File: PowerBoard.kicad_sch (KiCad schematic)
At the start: 106 parts, among them IC1 LT1910ES8#PBF, IC2 LT1910ES8#PBF, IC3 LT1910ES8#PBF, IC4 LT1910ES8#PBF, J1 XT90, J10 DEAN_T, J11 DEAN_T, J12 DEAN_T, J13 DEAN_T, J14 DEAN_T, J15 DEAN_T, J16 XT60, J17 XT60, J18 XT60, J19 XT60, J2 DEAN_T, J20 XT60, J21 XT60, J22 XT30, J23 XT30, J24 XT30, J25 XT30, J26 XT30, J27 XT30, J28 XT90, J29 XT30, J3 XT60, J30 XT30, J31 XT30, J32 Conn_01x02, J4 XT30, J5 XT90, J6 XT90, J7 XT90, J8 XT90, J9 XT90, Q1 IRFS7437TRLPBF, Q2 IRFS7437TRLPBF, Q3 IRFS7437TRLPBF, Q5 IRFS7530-7PPBF, U1 Pico, U2 LM317_TO-220

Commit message: Finish the design
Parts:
- removed A1, A2: ADS1115_ADC_Module, my_footprint_lib:ADS1115, symbol Charleslabs_Parts:ADS1115_ADC_Module
- removed ADC1, SPI1: Screw_Terminal_01x04, TerminalBlock:TerminalBlock_Xinya_XY308-2.54-4P_1x04_P2.54mm_Horizontal, symbol Connector:Screw_Terminal_01x04
- removed C2: 1u, Capacitor_SMD:C_1206_3216Metric, symbol Device:C
- removed C3, C4: 10u, Capacitor_Tantalum_SMD:CP_EIA-7343-15_Kemet-W, symbol Device:C_Polarized
- removed J14: DEAN_T, my_footprint_lib:DEAN_T, symbol Connector_Generic:Conn_01x02
- removed J26: XT30, my_footprint_lib:XT30, symbol Connector_Generic:Conn_01x02
- removed J6: XT90, my_footprint_lib:XT90, symbol Connector_Generic:Conn_01x02
- removed Q5: IRFS7530-7PPBF, IRFS41157PPBF, symbol SamacSys_Parts:IRFS7530-7PPBF
- removed R25, R27, R29, R32: 100k, Resistor_SMD:R_1206_3216Metric, symbol Device:R_US
- removed R26, R28, R31: 10k, Resistor_SMD:R_1206_3216Metric, symbol Device:R_US
- removed R30: 33k, Resistor_SMD:R_1206_3216Metric, symbol Device:R_US
- removed R35: 680R, Resistor_SMD:R_1206_3216Metric, symbol Device:R_US
- removed R36: 220R, Resistor_SMD:R_1206_3216Metric, symbol Device:R_US
- removed U2: LM317_TO-220, Package_TO_SOT_THT:TO-220-3_Vertical, symbol Regulator_Linear:LM317_TO-220
- added C10: 22pF, Capacitor_SMD:C_1206_3216Metric, symbol Device:C
- added C11: 3300pF, Capacitor_SMD:C_1206_3216Metric, symbol Device:C
- added C12: 10u, Capacitor_SMD:C_1206_3216Metric, symbol Device:C
- added C13, C7, C8: 1u, Capacitor_SMD:C_1206_3216Metric, symbol Device:C
- added C9: 5.5nF, Capacitor_SMD:C_1206_3216Metric, symbol Device:C
- added D10: SMAJ30CA, Diode_SMD:D_SMA, symbol Diode:SMAJ30CA
- added D3, D6: LED, Diode_SMD:D_1206_3216Metric, symbol Device:LED
- added F1: Fuse, Fuse:Fuse_Blade_ATO_directSolder, symbol Device:Fuse
- added H5: MountingHole, MountingHole:MountingHole_3.2mm_M3, symbol Mechanical:MountingHole
- added IC1: LT1910ES8#PBF, SOIC127P599X175-8N, symbol SamacSys_Parts:LT1910ES8#PBF
- added IC7: MAX17541GATB+T, SON50P200X300X80-11N, symbol SamacSys_Parts:MAX17541GATB+T
- added J10: XT90, SamacSys_Parts:XT90, symbol Connector_Generic:Conn_01x02
- added J16: DEAN_T, SamacSys_Parts:DEANS-T, symbol Connector_Generic:Conn_01x02
- added J22, J41: XT60, Connector_AMASS:AMASS_XT60-F_1x02_P7.20mm_Vertical, symbol Connector_Generic:Conn_01x02
- added J32, J34, J35, J36, J37, J38, J39, J40: XT30, Connector_AMASS:AMASS_XT30U-F_1x02_P5.0mm_Vertical, symbol Connector_Generic:Conn_01x02
- added L1: 470M, SRR5828A2R6Y, symbol SamacSys_Parts:SRR5828A-470M
- added Q1: IRFS7530TRL7PP, IRFS7530TRL7PP, symbol SamacSys_Parts:IRFS7530TRL7PP
- added Q2: IRFS7437TRLPBF, Package_TO_SOT_SMD:TO-263-2, symbol Transistor_FET:IRF9540N
- added R16: 80k, Resistor_SMD:R_1206_3216Metric, symbol Device:R
- added R17: 17.5k, Resistor_SMD:R_1206_3216Metric, symbol Device:R
- added R18, R19, R20, R26, R27, R28, R29: 10k, Resistor_SMD:R_1206_3216Metric, symbol Device:R
- added R2, R5: 6k8, Resistor_SMD:R_1206_3216Metric, symbol Device:R_US
- added R21: 21.5k, Resistor_SMD:R_1206_3216Metric, symbol Device:R
- added R7: 5m, RESC3216X89N, symbol SamacSys_Parts:WSL12061L000FEA
- added U2, U3, U4, U5, U6: INA238, Package_SO:VSSOP-10_3x3mm_P0.5mm, symbol Sensor_Energy:INA238
- J1, J7, J8, J9: footprint my_footprint_lib:XT90 -> SamacSys_Parts:XT90
- J11, J12, J13: value DEAN_T -> XT90; footprint my_footprint_lib:DEAN_T -> SamacSys_Parts:XT90
- J14: renamed from J10; footprint my_footprint_lib:DEAN_T -> SamacSys_Parts:DEANS-T
- J15, J2: footprint my_footprint_lib:DEAN_T -> SamacSys_Parts:DEANS-T
- J17, J18, J19: value XT60 -> DEAN_T; footprint Connector_AMASS:AMASS_XT60-F_1x02_P7.20mm_Vertical -> SamacSys_Parts:DEANS-T
- J23, J24, J25, J27, J29, J30, J31: value XT30 -> XT60; footprint my_footprint_lib:XT30 -> Connector_AMASS:AMASS_XT60-F_1x02_P7.20mm_Vertical
- J28: value XT90 -> XT60; footprint my_footprint_lib:XT90 -> Connector_AMASS:AMASS_XT60-F_1x02_P7.20mm_Vertical
- J3: footprint my_footprint_lib:XT60 -> Connector_AMASS:AMASS_XT60-F_1x02_P7.20mm_Vertical
- J33: renamed from J22; footprint my_footprint_lib:XT30 -> Connector_AMASS:AMASS_XT30U-F_1x02_P5.0mm_Vertical
- J4: footprint my_footprint_lib:XT30 -> Connector_AMASS:AMASS_XT30U-F_1x02_P5.0mm_Vertical
- J5: renamed from J32; footprint my_footprint_lib:XT90 -> SamacSys_Parts:XT90
- J6: renamed from J5; footprint my_footprint_lib:XT90 -> SamacSys_Parts:XT90
- renumbered C7 to C2, C8 to C3, C6 to C4, D6 to D1, D3 to D11, D11 to D12, D10 to D13, D4 to D14, D12 to D15, D17 to D16, D1 to D17, D15 to D18, D16 to D19, D7 to D4, D13 to D5, D8 to D7, D14 to D8, D5 to D9, F1 to F2, F4 to F3, F3 to F4, F2 to F5, H4 to H1, H1 to H2, H2 to H3, H3 to H4, IC3 to IC2, IC4 to IC3, IC2 to IC4, IC1 to IC5, J16 to J26, Q2 to Q3, Q3 to Q4, Q1 to Q5, R7 to R1, R3 to R10, R8 to R11, R9 to R12, R4 to R13, R11 to R14, R10 to R15, R33 to R22, R39 to R23, R40 to R24, R1 to R3, R5 to R4, R2 to R6, R12 to R8, R6 to R9
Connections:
- net +12V: now also J3.2 (Pin_2), U5.10 (Vin+), U5.8 (Vbus); no longer J3.1 (Pin_1)
- net +24V: now also J2.2 (Pin_2), U3.10 (Vin+), U3.8 (Vbus); no longer J2.1 (Pin_1)
- net +42V: now also C7.1, IC7.2 (VIN), IC7.3 (EN/UVLO); no longer C1.1
- net +5V: now also U6.10 (Vin+), U6.8 (Vbus)
- net 12V_2: now also J27.2 (Pin_2), J28.2 (Pin_2), J29.2 (Pin_2), J30.2 (Pin_2), J31.2 (Pin_2); no longer J17.2 (Pin_2), J18.2 (Pin_2), J19.2 (Pin_2), J20.2 (Pin_2), J21.2 (Pin_2)
- net 24V_2: now also J14.2 (Pin_2), J15.2 (Pin_2), J17.2 (Pin_2), J18.2 (Pin_2), J19.2 (Pin_2), J16.2 (Pin_2); no longer J11.1 (Pin_1), J12.1 (Pin_1), J13.1 (Pin_1), J14.1 (Pin_1), J15.1 (Pin_1)
- net 42V_2: now also J11.1 (Pin_1), J12.1 (Pin_1), J13.1 (Pin_1), J10.1 (Pin_1); no longer J28.1 (Pin_1)
- net 5V_2: now also D14.1 (A1), J33.2 (Pin_2), J32.2 (Pin_2), J34.2 (Pin_2), J35.2 (Pin_2), J36.2 (Pin_2), J37.2 (Pin_2), J38.2 (Pin_2), J39.2 (Pin_2), J40.2 (Pin_2); no longer D14.2 (A2), J23.1 (Pin_1), J24.1 (Pin_1), J25.1 (Pin_1), J27.1 (Pin_1), J29.1 (Pin_1), J30.1 (Pin_1), J31.1 (Pin_1), J33.1 (Pin_1)
- net EN_12V: now also U1.14 (GPIO10); no longer U1.10 (GPIO7)
- net EN_24V: now also U1.16 (GPIO12); no longer U1.11 (GPIO8)
- net EN_42V: now also U1.17 (GPIO13); no longer U1.12 (GPIO9)
- net EN_5V: now also U1.12 (GPIO9); no longer U1.9 (GPIO6)
- net GND: now also D14.2 (A2), J14.1 (Pin_1), J15.1 (Pin_1), J2.1 (Pin_1), J23.1 (Pin_1), J24.1 (Pin_1), J25.1 (Pin_1), J27.1 (Pin_1), J28.1 (Pin_1), J29.1 (Pin_1), J3.1 (Pin_1), J30.1 (Pin_1), J31.1 (Pin_1), J33.1 (Pin_1), C10.2, C11.2, C12.2, C13.2, C7.2, C8.2, C9.2, D10.1 (A1), IC1.1 (GND), IC7.1 (PGND), IC7.11 (EP), IC7.9 (GND), J10.2 (Pin_2), J16.1 (Pin_1), J22.1 (Pin_1), J32.1 (Pin_1), J34.1 (Pin_1), J35.1 (Pin_1), J36.1 (Pin_1), J37.1 (Pin_1), J38.1 (Pin_1), J39.1 (Pin_1), J40.1 (Pin_1), J41.1 (Pin_1), R17.2, R2.2, R5.2, U2.1 (A1), U2.2 (A0), U2.7 (GND), U3.1 (A1), U3.7 (GND), U4.1 (A1), U4.7 (GND), U5.1 (A1), U5.7 (GND), U6.2 (A0), U6.7 (GND); no longer D14.1 (A1), J14.2 (Pin_2), J15.2 (Pin_2), J2.2 (Pin_2), J23.2 (Pin_2), J24.2 (Pin_2), J25.2 (Pin_2), J27.2 (Pin_2), J28.2 (Pin_2), J29.2 (Pin_2), J3.2 (Pin_2), J30.2 (Pin_2), J31.2 (Pin_2), J33.2 (Pin_2)
- net SCL: now also R19.2, U2.5 (SCL), U3.5 (SCL), U4.5 (SCL), U5.2 (A0), U5.5 (SCL), U6.5 (SCL)
- net SDA: now also R18.2, U2.4 (SDA), U3.4 (SDA), U4.2 (A0), U4.4 (SDA), U5.4 (SDA), U6.4 (SDA)
- net VCC: now also C12.1, C13.1, L1.2, R16.1, R18.1, R19.1, R20.1, R26.1, R27.1, R28.1, R29.1, U2.6 (VS), U3.2 (A0), U3.6 (VS), U4.6 (VS), U5.6 (VS), U6.1 (A1), U6.6 (VS)
- net CURR_1+: now reaches IC3.8 (V+), R1.2
- net CURR_1+: now also U2.10 (Vin+), U2.8 (Vbus)
- net CURR_1-: now reaches IC3.6 (SENSE), R1.3
- net CURR_1-: now also U2.9 (Vin-)
- net at R1.4: now also Q1.4 (D)
- net ALERT_5: now reaches U1.24 (GPIO18)
- net ALERT_5: now also R29.2, U6.3 (~{Alert})
- net ALERT_4: now reaches U1.22 (GPIO17)
- net ALERT_4: now also R28.2, U5.3 (~{Alert})
- net ALERT_3: now reaches U1.21 (GPIO16)
- net ALERT_3: now also R27.2, U4.3 (~{Alert})
- net at D5.2 (A), F3.1: now also Q1.2 (S_1), Q1.3 (S_2), Q1.5 (S_3), Q1.6 (S_4), Q1.7 (S_5)
- net FAULT_24V: now reaches IC5.3 (~{FAULT})
- net FAULT_24V: now also U1.5 (GPIO3)
- net CURR_2-: now reaches IC5.6 (SENSE), Q5.3 (S), R11.1
- net CURR_2-: now also U3.9 (Vin-)
- net EN_15V: now reaches U1.15 (GPIO11)
- net EN_15V: now also IC1.4 (IN)
- net ALERT_1: now reaches U1.19 (GPIO14)
- net ALERT_1: now also R20.2, U2.3 (~{Alert})
- net ALERT_2: now reaches U1.20 (GPIO15)
- net ALERT_2: now also R26.2, U3.3 (~{Alert})
- net FAULT_42V: now reaches U1.4 (GPIO2)
- net FAULT_42V: now also IC3.3 (~{FAULT})
- net CURR_4-: now reaches IC4.6 (SENSE), Q4.3 (S), R14.2
- net CURR_4-: now also U5.9 (Vin-)
- net at IC3.5 (GATE): now also Q1.1 (G)
- net FAULT_12V: now reaches IC4.3 (~{FAULT})
- net FAULT_12V: now also U1.10 (GPIO7)
- net FAULT_5V: now reaches IC2.3 (~{FAULT})
- net FAULT_5V: now also U1.11 (GPIO8)
- net CURR_5-: now reaches IC2.6 (SENSE), Q3.3 (S), R8.2
- net CURR_5-: now also U6.9 (Vin-)
- new net: D6.1 (K), R5.1
- new net: IC7.5 (FB), R16.2, R17.1
- new net: C8.1, IC7.4 (VCC)
- new net: D3.1 (K), R2.1
- new net: C10.1, IC7.7 (COMP), R21.1
- new net: C11.1, R21.2
- new net: D3.2 (A), F1.1, Q2.2 (D)
- new net: C9.1, IC7.6 (SS)
- new net: C1.1, IC1.2 (TIMER)
- new net: IC1.5 (GATE), Q2.1 (G)
- new net: IC7.10 (LX), L1.1
- new net +15V: IC1.8 (V+), J41.2 (Pin_2), R7.1, U4.10 (Vin+), U4.8 (Vbus)
- new net 15V_2: D10.2 (A2), D6.2 (A), F1.2, J20.2 (Pin_2), J21.2 (Pin_2), J22.2 (Pin_2), J23.2 (Pin_2), J24.2 (Pin_2), J25.2 (Pin_2)
- new net CURR_3-: IC1.6 (SENSE), Q2.3 (S), R7.2, U4.9 (Vin-)
- new net FAULT_15V: IC1.3 (~{FAULT}), U1.9 (GPIO6)
- no-connect marks 24 -> 13
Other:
- note added: "12V High-Side Switch"
- note added: "15V High-Side Switch"
- note added: "24V High-Side Switch"
- note added: "5V AUX Switched Power Supply"
- note added: "5V High-Side Switch"
- note added: "Aux Connectors"
- note added: "Battery Voltage High-Side Switch"
- note added: "Microprocessor"
- note added: "Voltage Input Connectors"
- note added: "Voltage Output Connectors"
- note added: "Voltage/Current/Power/Energy Measurement"
- moved on the sheet: C2, C3, C4, C5, D1, D11, D12, D13, D14, D15, D16, D17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

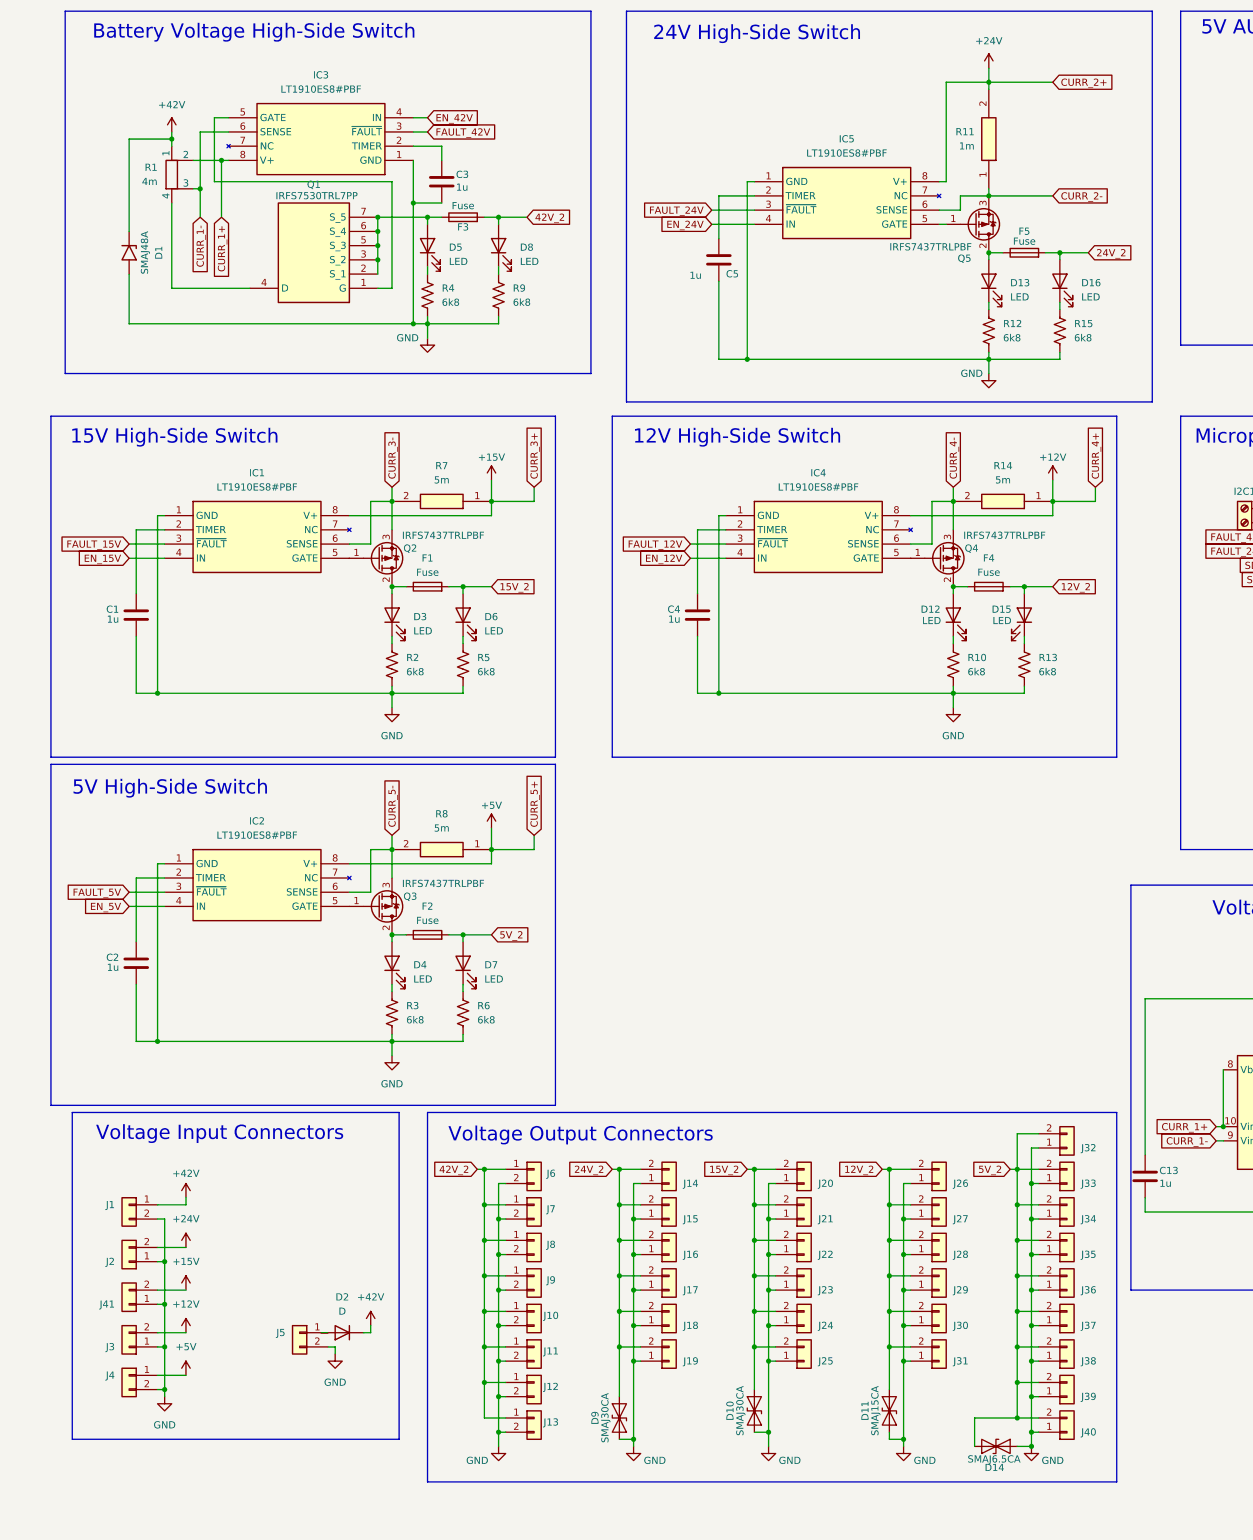
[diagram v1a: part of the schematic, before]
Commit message: add base resistors for the power mosfets
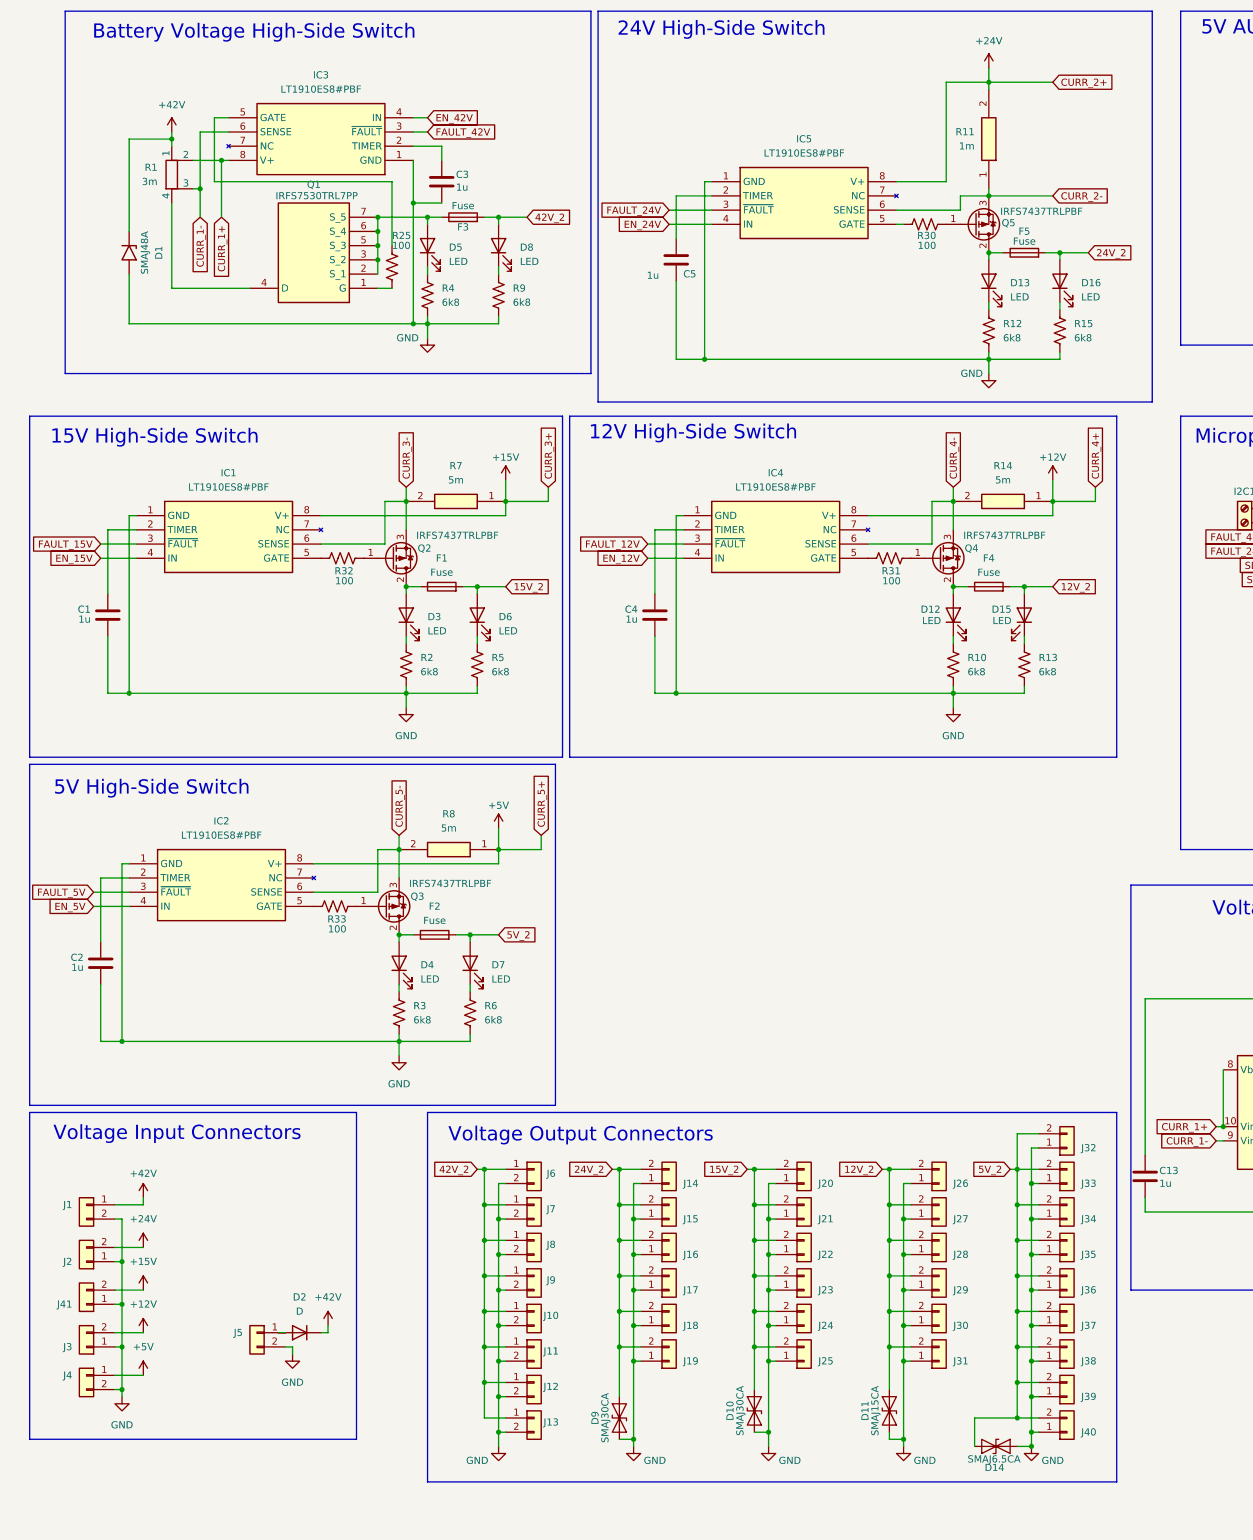
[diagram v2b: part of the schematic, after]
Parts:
- added R25, R30, R31, R32, R33: 100, Resistor_SMD:R_1206_3216Metric, symbol Device:R_US
- R1: value 4m -> 3m
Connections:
- net at IC5.5 (GATE): now also R30.1; no longer Q5.1 (G)
- net at IC3.5 (GATE): now also R25.1; no longer Q1.1 (G)
- net at IC4.5 (GATE): now also R31.1; no longer Q4.1 (G)
- net at Q2.1 (G): now also R32.2; no longer IC1.5 (GATE)
- net at IC2.5 (GATE): now also R33.1; no longer Q3.1 (G)
- new net: Q5.1 (G), R30.2
- new net: IC1.5 (GATE), R32.1
- new net: Q1.1 (G), R25.2
- new net: Q4.1 (G), R31.2
- new net: Q3.1 (G), R33.2
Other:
- moved on the sheet: C1, C2, C4, C5, D2, D3, D4, D6, D7, F1, F2, IC1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

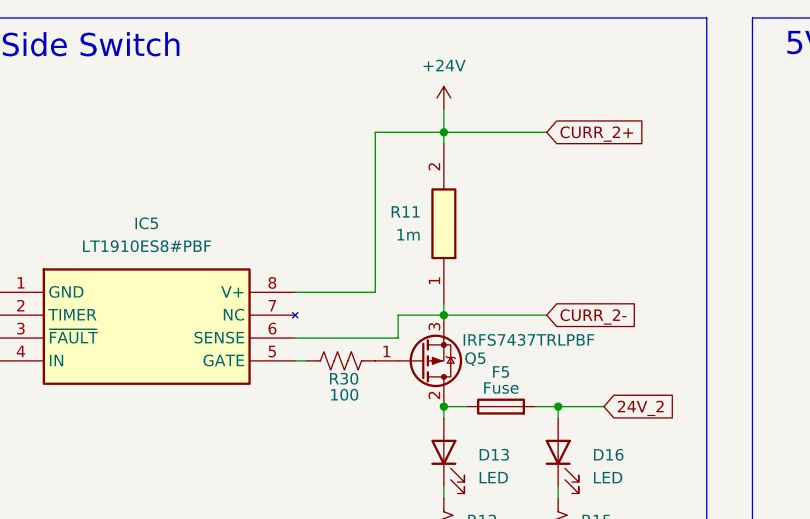
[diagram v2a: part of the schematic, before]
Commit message: change shunt value
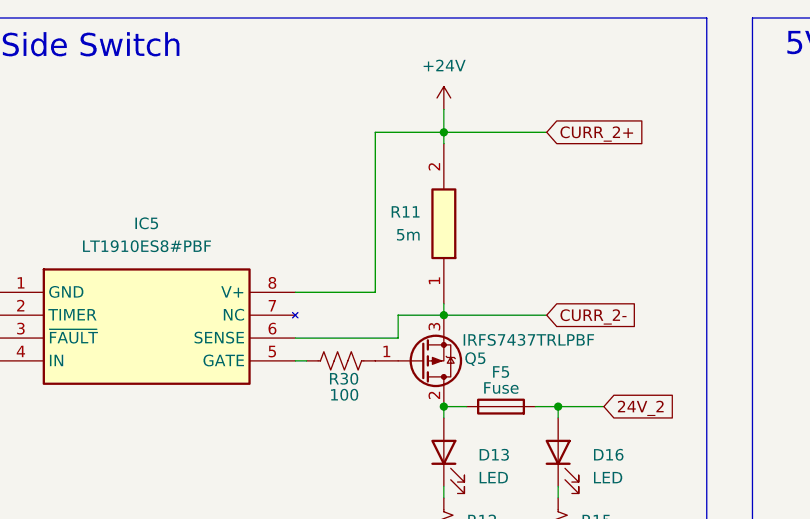
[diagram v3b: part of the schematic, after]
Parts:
- R11: value 1m -> 5m
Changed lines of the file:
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@@
 			)
 		)
-		(property "Value" "1m"
+		(property "Value" "5m"
 			(at 181.61 45.7199 90)
 			(effects

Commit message: Adjust resistor and transil values
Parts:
- D1: value SMAJ48A -> SMAJ43A
- D10: value SMAJ30CA -> SMAJ15A
- D11: value SMAJ15CA -> SMAJ12A
- D14: value SMAJ6.5CA -> SMAJ5A
- D9: value SMAJ30CA -> SMAJ24A
- R10, R13, R2, R5: value 6k8 -> 2k2
- R12, R15: value 6k8 -> 4k7
- R16: value 80k -> 82k5
- R17: value 17.5k -> 18k2
- R22, R23, R24: value 10k -> 2k2
- R3, R6: value 6k8 -> 470
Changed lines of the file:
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@@
 		(at 288.29 118.11)
 	)
-	(bus_entry
-		(at 265.43 302.26)
-		(size 2.54 2.54)
-		(stroke
-			(width 0)
-			(type default)
-		)
-	)
 	(wire
 		(pts
@@
 	(rectangle
 		(start 341.63 93.98)
-		(end 400.05 143.51)
+		(end 374.65 143.51)
 		(stroke
 			(width 0)
@@
 			)
 		)
-		(property "Value" "6k8"
+		(property "Value" "2k2"
 			(at 193.04 139.6999 0)
 			(effects
@@
 			)
 		)
-		(property "Value" "80k"
-			(at 237.236 49.53 0)
+		(property "Value" "82k5"
+			(at 236.22 49.53 0)
 			(effects
 				(font
@@
 			)
 		)
-		(property "Value" "6k8"
+		(property "Value" "4k7"
 			(at 199.39 80.0099 0)
 			(effects
@@
 			)
 		)
-		(property "Value" "6k8"
+		(property "Value" "2k2"
 			(at 82.55 139.6999 0)
 			(effects
@@
 			)
 		)
-		(property "Value" "SMAJ30CA"
+		(property "Value" "SMAJ24A"
 			(at 115.57 273.05 0)
 			(effects
@@
 			)
 		)
-		(property "Value" "SMAJ6.5CA"
-			(at 180.34 280.416 0)
+		(property "Value" "SMAJ5A"
+			(at 181.356 280.416 0)
 			(effects
 				(font
@@
 			)
 		)
-		(property "Value" "SMAJ48A"
+		(property "Value" "SMAJ43A"
 			(at 33.274 64.77 0)
 			(effects
@@
 			)
 		)
-		(property "Value" "17.5k"
-			(at 235.458 57.658 0)
+		(property "Value" "18k2"
+			(at 236.22 57.404 0)
 			(effects
 				(font
@@
 			)
 		)
-		(property "Value" "10k"
+		(property "Value" "2k2"
 			(at 317.5 113.03 90)
 			(effects
@@
 			)
 		)
-		(property "Value" "10k"
+		(property "Value" "2k2"
 			(at 317.5 123.19 90)
 			(effects
@@
 			)
 		)
-		(property "Value" "SMAJ15CA"
+		(property "Value" "SMAJ12A"
 			(at 163.83 271.78 0)
 			(effects
@@
 			)
 		)
-		(property "Value" "6k8"
+		(property "Value" "470"
 			(at 93.98 201.9299 0)
 			(effects
@@
 			)
 		)
-		(property "Value" "6k8"
+		(property "Value" "2k2"
 			(at 95.25 139.6999 0)
 			(effects
@@
 			)
 		)
-		(property "Value" "SMAJ30CA"
+		(property "Value" "SMAJ15A"
 			(at 139.7 271.78 0)
 			(effects
@@
 			)
 		)
-		(property "Value" "6k8"
+		(property "Value" "470"
 			(at 81.28 201.9299 0)
 			(effects
@@
 			)
 		)
-		(property "Value" "10k"
+		(property "Value" "2k2"
 			(at 317.5 133.35 90)
 			(effects
@@
 			)
 		)
-		(property "Value" "6k8"
+		(property "Value" "2k2"
 			(at 180.34 139.6999 0)
 			(effects
@@
 			)
 		)
-		(property "Value" "6k8"
+		(property "Value" "4k7"
 			(at 186.69 80.0099 0)
 			(effects

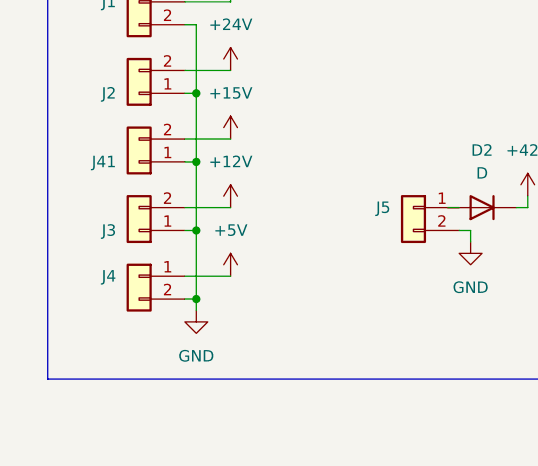
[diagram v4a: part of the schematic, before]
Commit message: remove solder mask from high current traces and optimize vias for cheaper manufacturing process
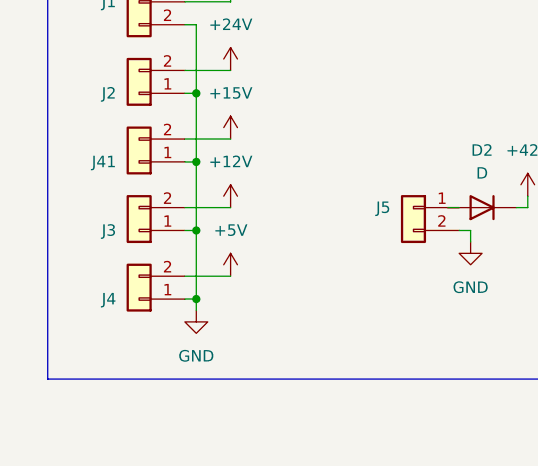
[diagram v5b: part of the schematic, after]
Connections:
- net +5V: now also J4.2 (Pin_2); no longer J4.1 (Pin_1)
- net GND: now also J4.1 (Pin_1); no longer J4.2 (Pin_2)
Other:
- moved on the sheet: J4
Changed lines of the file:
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@@
 	(wire
 		(pts
+			(xy 27.94 265.43) (xy 33.02 265.43)
+		)
+		(stroke
+			(width 0)
+			(type default)
+		)
+	)
+	(wire
+		(pts
 			(xy 176.53 34.29) (xy 184.15 34.29)
 		)
@@
 	(wire
 		(pts
-			(xy 27.94 265.43) (xy 33.02 265.43)
-		)
-		(stroke
-			(width 0)
-			(type default)
-		)
-	)
-	(wire
-		(pts
 			(xy 24.13 179.07) (xy 30.48 179.07)
 		)
@@
 	(symbol
 		(lib_id "Connector_Generic:Conn_01x02")
-		(at 22.86 265.43 0)
-		(mirror y)
+		(at 22.86 267.97 180)
 		(unit 1)
 		(exclude_from_sim no)
@@
 		(on_board yes)
 		(dnp no)
-		(fields_autoplaced yes)
 		(property "Reference" "J4"
-			(at 20.32 265.43 0)
+			(at 20.32 267.97 0)
 			(effects
 				(font
@@
 		)
 		(property "Value" "XT30"
-			(at 20.32 267.97 0)
+			(at 20.32 265.43 0)
 			(effects
 				(font
@@
 		)
 		(property "Footprint" "Connector_AMASS:AMASS_XT30U-F_1x02_P5.0mm_Vertical"
-			(at 22.86 265.43 0)
+			(at 22.86 267.97 0)
 			(effects
 				(font
@@
 		)
 		(property "Datasheet" "~"
-			(at 22.86 265.43 0)
+			(at 22.86 267.97 0)
 			(effects
 				(font
@@
 		)
 		(property "Description" "Generic connector, single row, 01x02, script generated (kicad-library-utils/schlib/autogen/connector/)"
-			(at 22.86 265.43 0)
+			(at 22.86 267.97 0)
 			(effects
 				(font
